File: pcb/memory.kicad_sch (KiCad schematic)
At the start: 2 parts, among them U6 MT41K256M16LY, U8 MX25L3233FZN

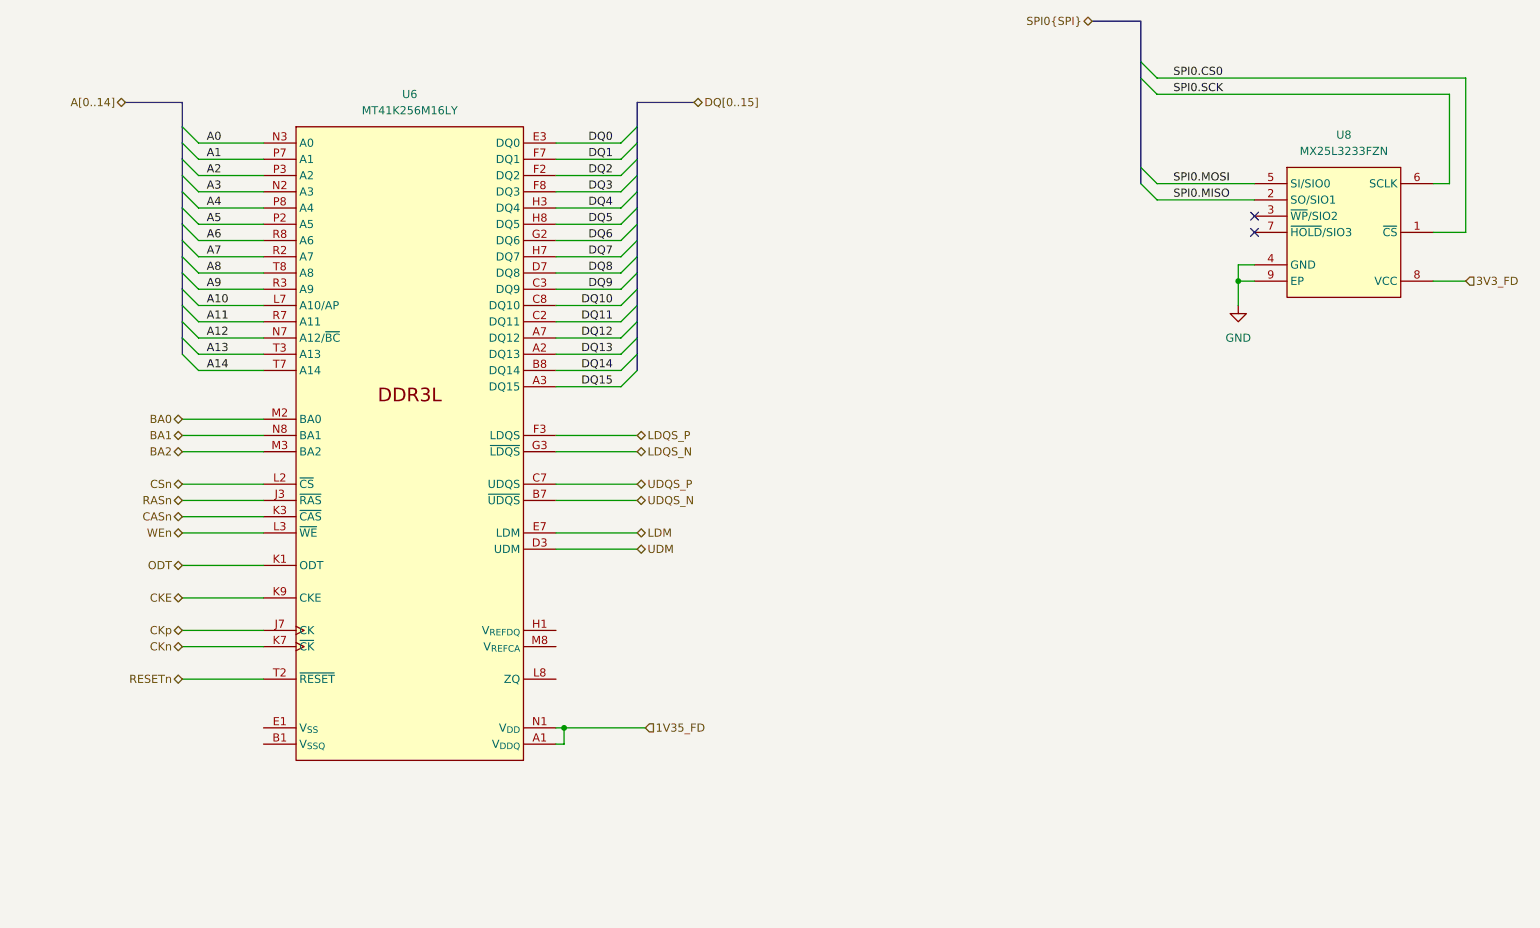
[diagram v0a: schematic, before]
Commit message: changes to power tree
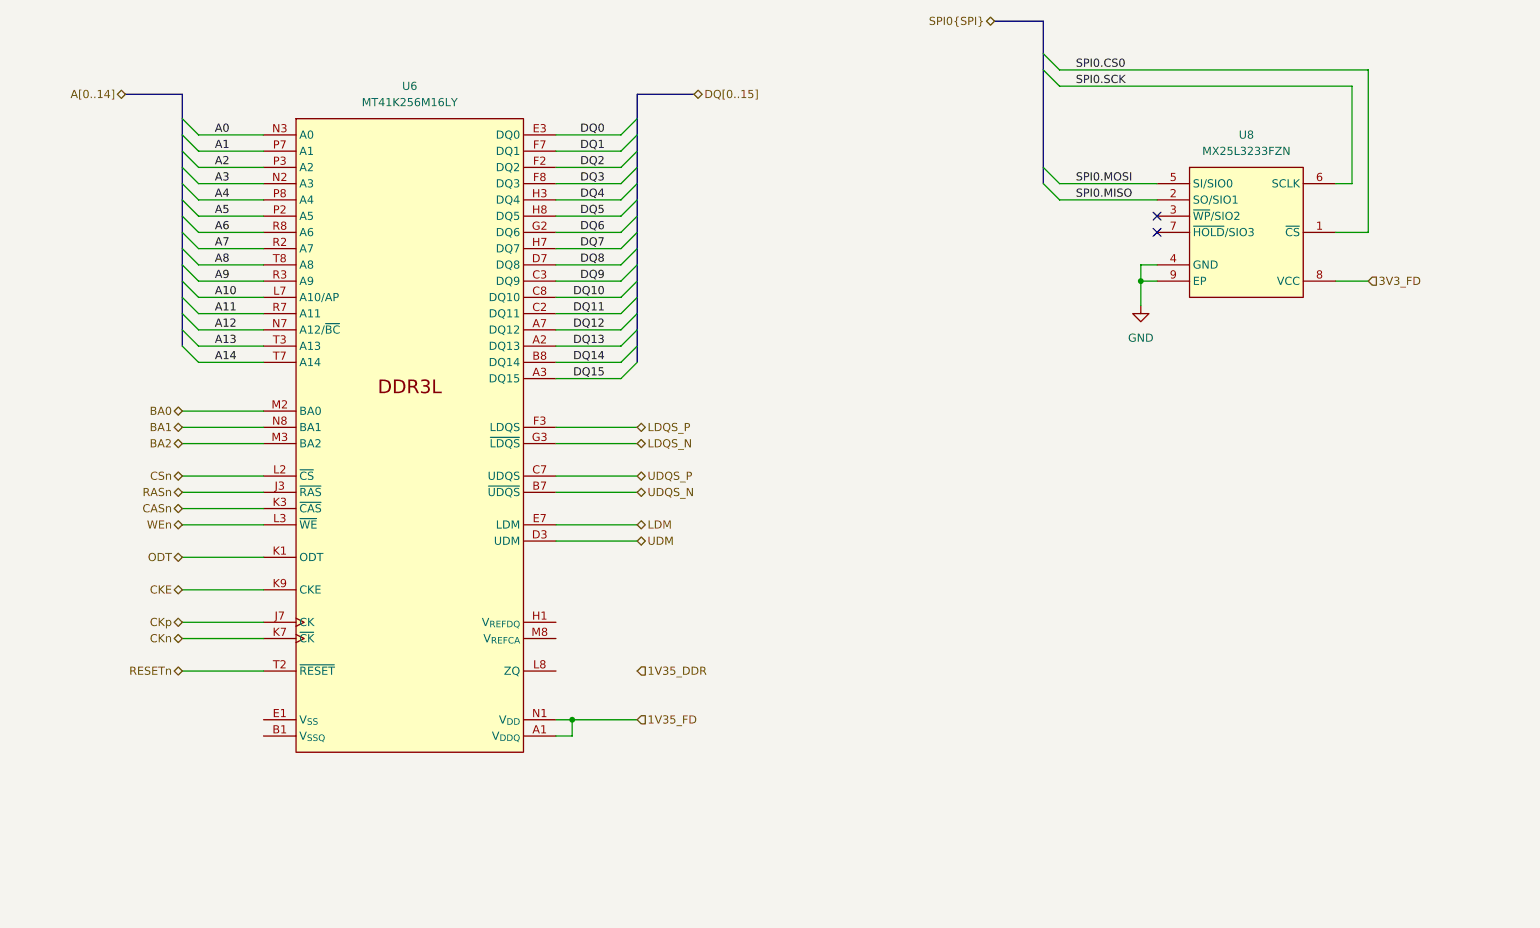
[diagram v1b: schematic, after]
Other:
- moved on the sheet: U6, U8

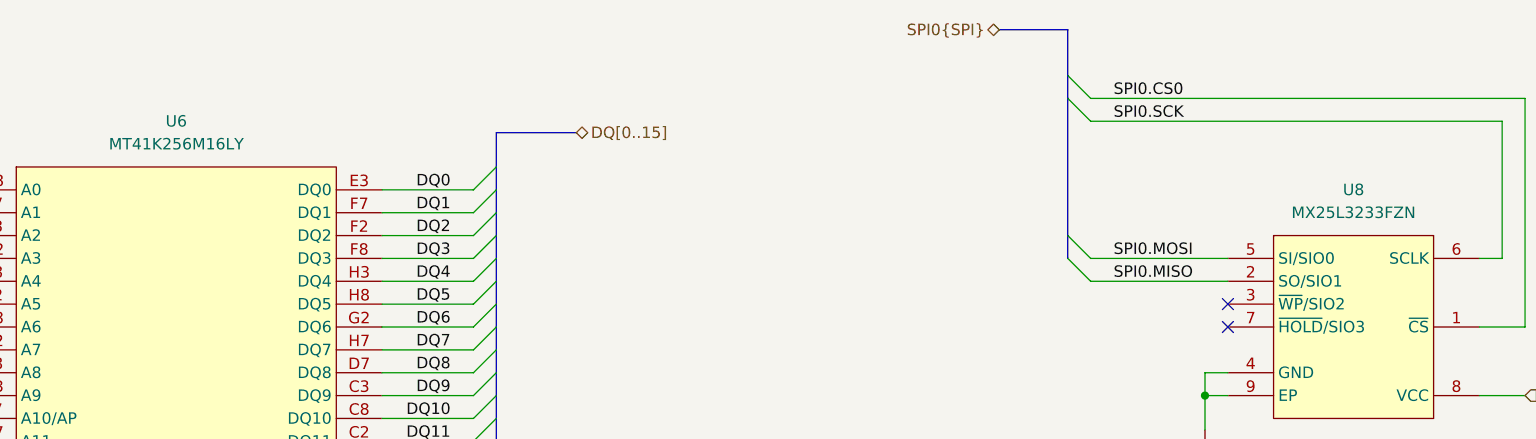
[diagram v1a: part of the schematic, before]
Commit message: moved stuff around, bom
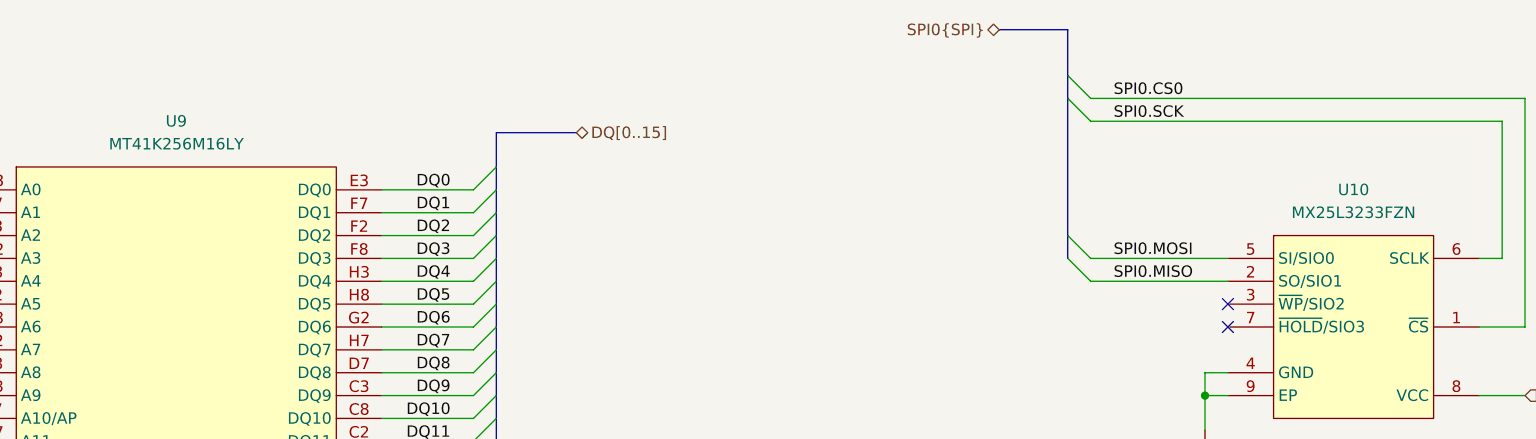
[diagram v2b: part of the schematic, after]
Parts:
- renumbered U8 to U10, U6 to U9
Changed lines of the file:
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@@
 		(dnp no)
 		(fields_autoplaced yes)
-		(property "Reference" "U8"
+		(property "Reference" "U10"
 			(at 237.49 43.18 0)
 			(effects
@@
 			(project ""
 				(path "/e63e39d7-6ac0-4ffd-8aa3-1841a4541b55/59d21473-a004-4514-8090-fd93db818925/b633a666-4c3d-4ac9-9e0f-b350177ade0b"
-					(reference "U8")
+					(reference "U10")
 					(unit 1)
 				)
@@
 		(dnp no)
 		(fields_autoplaced yes)
-		(property "Reference" "U6"
+		(property "Reference" "U9"
 			(at 106.68 35.56 0)
 			(effects
@@
 			(project ""
 				(path "/e63e39d7-6ac0-4ffd-8aa3-1841a4541b55/59d21473-a004-4514-8090-fd93db818925/b633a666-4c3d-4ac9-9e0f-b350177ade0b"
-					(reference "U6")
+					(reference "U9")
 					(unit 1)
 				)

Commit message: qspi
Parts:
- U10: value MX25L3233FZN -> MX25L12835F
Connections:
- net 1V35_FD is gone; now on net 1V35_DDR: U9.A1 (V_{DDQ}), U9.A8 (V_{DDQ}), U9.B2 (V_{DD}), U9.C1 (V_{DDQ}), U9.C9 (V_{DDQ}), U9.D2 (V_{DDQ}), U9.D9 (V_{DD}), U9.E9 (V_{DDQ}), U9.F1 (V_{DDQ}), U9.G7 (V_{DD}), U9.H2 (V_{DDQ}), U9.H9 (V_{DDQ}), U9.K2 (V_{DD}), U9.K8 (V_{DD}), U9.N1 (V_{DD}), U9.N9 (V_{DD}), U9.R1 (V_{DD}), U9.R9 (V_{DD})
- net QSPI0.SIO2: now reaches U10.3 (~{WP}/SIO2)
- net QSPI0.SIO3: now reaches U10.7 (~{HOLD}/SIO3)
- net SPI0.CS0 renamed QSPI0.CS0n
- net SPI0.MISO renamed QSPI0.SIO1
- net SPI0.MOSI renamed QSPI0.SIO0
- net SPI0.SCK renamed QSPI0.SCLK
- no-connect marks 2 -> 0
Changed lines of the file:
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@@
 		(company "Andre S Winkel")
+	)
+	(bus_alias "QSPI"
+		(members "SIO0" "SIO1" "SIO2" "SIO3" "SCLK" "CS0n" "CS1n")
 	)
 	(junction
@@
 		(color 0 0 0 0)
 	)
-	(no_connect
-		(at 223.52 58.42)
-	)
-	(no_connect
-		(at 223.52 55.88)
-	)
 	(bus_entry
 		(at 139.7 53.34)
@@
 	)
 	(bus_entry
+		(at 205.74 55.88)
+		(size 2.54 2.54)
+		(stroke
+			(width 0)
+			(type default)
+		)
+	)
+	(bus_entry
 		(at 73.66 58.42)
 		(size -2.54 -2.54)
@@
 	)
 	(bus_entry
+		(at 205.74 53.34)
+		(size 2.54 2.54)
+		(stroke
+			(width 0)
+			(type default)
+		)
+	)
+	(bus_entry
 		(at 73.66 45.72)
 		(size -2.54 -2.54)
@@
 	(wire
 		(pts
+			(xy 208.28 58.42) (xy 223.52 58.42)
+		)
+		(stroke
+			(width 0)
+			(type default)
+		)
+	)
+	(wire
+		(pts
 			(xy 71.12 121.92) (xy 83.82 121.92)
 		)
@@
 	(bus
 		(pts
+			(xy 205.74 50.8) (xy 205.74 53.34)
+		)
+		(stroke
+			(width 0)
+			(type default)
+		)
+	)
+	(bus
+		(pts
 			(xy 71.12 58.42) (xy 71.12 55.88)
 		)
@@
 		)
 	)
+	(wire
+		(pts
+			(xy 208.28 55.88) (xy 223.52 55.88)
+		)
+		(stroke
+			(width 0)
+			(type default)
+		)
+	)
 	(bus
 		(pts
@@
 		)
 	)
+	(bus
+		(pts
+			(xy 205.74 53.34) (xy 205.74 55.88)
+		)
+		(stroke
+			(width 0)
+			(type default)
+		)
+	)
 	(wire
 		(pts
@@
 		)
 	)
-	(label "SPI0.CS0"
+	(label "QSPI0.CS0n"
 		(at 210.82 33.02 0)
 		(effects
@@
 		)
 	)
-	(label "SPI0.SCK"
+	(label "QSPI0.SIO3"
+		(at 210.82 58.42 0)
+		(effects
+			(font
+				(size 1.27 1.27)
+			)
+			(justify left bottom)
+		)
+	)
+	(label "QSPI0.SIO2"
+		(at 210.82 55.88 0)
+		(effects
+			(font
+				(size 1.27 1.27)
+			)
+			(justify left bottom)
+		)
+	)
+	(label "QSPI0.SCLK"
 		(at 210.82 35.56 0)
 		(effects
@@
 		)
 	)
-	(label "SPI0.MOSI"
+	(label "QSPI0.SIO0"
 		(at 210.82 50.8 0)
 		(effects
@@
 		)
 	)
-	(label "SPI0.MISO"
+	(label "QSPI0.SIO1"
 		(at 210.82 53.34 0)
 		(effects
@@
 		)
 	)
-	(hierarchical_label "SPI0{SPI}"
+	(hierarchical_label "QSPI0{QSPI}"
 		(shape bidirectional)
 		(at 198.12 25.4 180)
@@
 		)
 	)
-	(hierarchical_label "1V35_FD"
+	(hierarchical_label "1V35_DDR"
 		(shape input)
 		(at 142.24 134.62 0)
@@
 			)
 			(justify right)
-		)
-	)
-	(hierarchical_label "1V35_DDR"
-		(shape input)
-		(at 142.24 127 0)
-		(effects
-			(font
-				(size 1.27 1.27)
-			)
-			(justify left)
 		)
 	)
@@
 			)
 		)
-		(property "Value" "MX25L3233FZN"
+		(property "Value" "MX25L12835F"
 			(at 237.49 45.72 0)
 			(effects

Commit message: bom
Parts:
- added R26: 240 1%, Resistor_SMD:R_0402_1005Metric, symbol library:R_US
- U10: Manufacturer (none) -> Macronix; Manufacturer Product Number (none) -> MX25L12835FZNI-10G; Part Description (none) -> IC FLASH 128MBIT SPI 8WSON
- U9: value MT41K256M16LY -> MT41K256M16TW-107:P TR; Manufacturer (none) -> Micron Technology Inc.; Manufacturer Product Number (none) -> MT41K256M16TW-107:P TR; Part Description (none) -> IC DRAM 4GBIT PAR 96FBGA
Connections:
- net 1V35_DDR: now also R26.2
- net GND: now also U9.A9 (V_{SS}), U9.B1 (V_{SSQ}), U9.B3 (V_{SS}), U9.B9 (V_{SSQ}), U9.D1 (V_{SSQ}), U9.D8 (V_{SSQ}), U9.E1 (V_{SS}), U9.E2 (V_{SSQ}), U9.E8 (V_{SSQ}), U9.F9 (V_{SSQ}), U9.G1 (V_{SSQ}), U9.G8 (V_{SS}), U9.G9 (V_{SSQ}), U9.J2 (V_{SS}), U9.J8 (V_{SS}), U9.M1 (V_{SS}), U9.M9 (V_{SS}), U9.P1 (V_{SS}), U9.P9 (V_{SS}), U9.T1 (V_{SS}), U9.T9 (V_{SS})
- net at U9.L8 (ZQ): now also R26.1

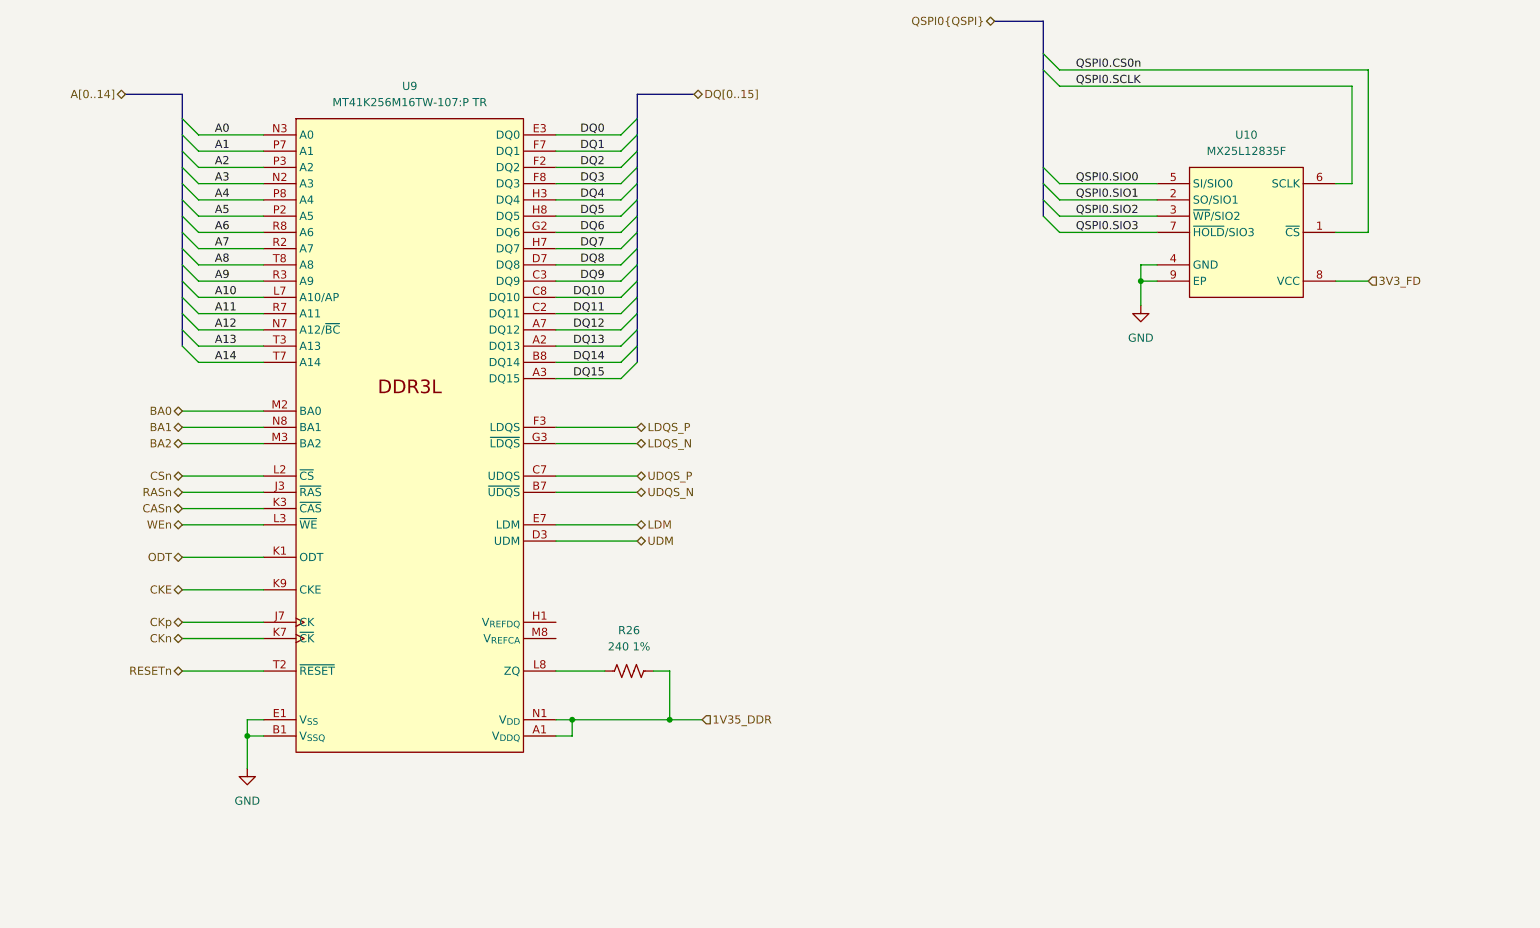
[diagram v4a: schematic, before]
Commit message: added mig ddr pinout constraints
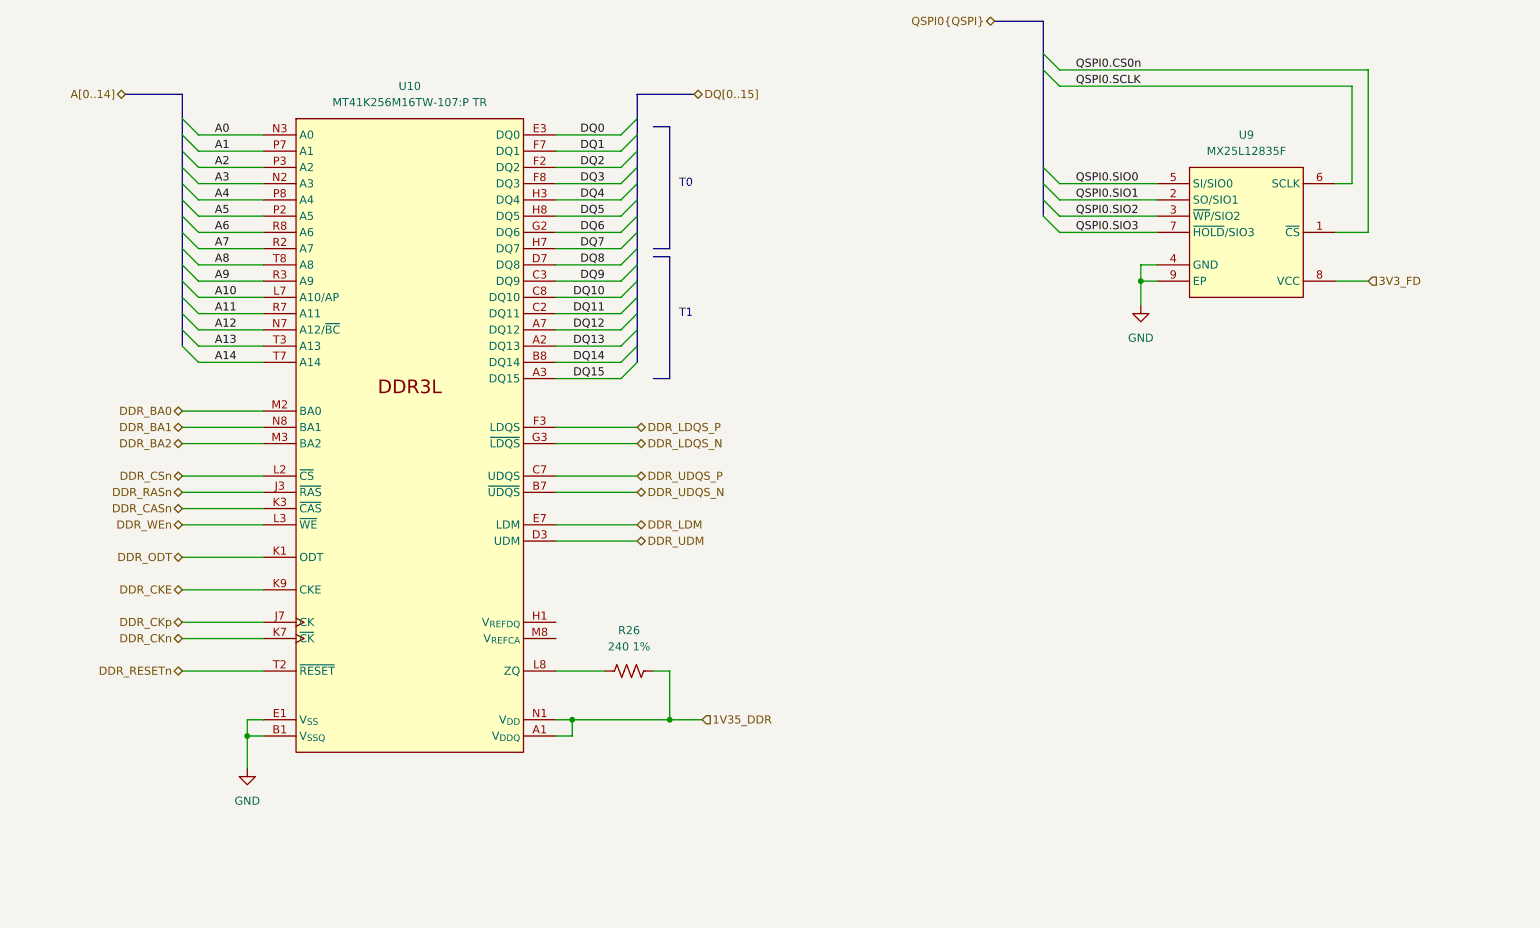
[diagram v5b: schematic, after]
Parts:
- renumbered U9 to U10, U10 to U9
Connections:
- net BA0 renamed DDR_BA0
- net BA1 renamed DDR_BA1
- net BA2 renamed DDR_BA2
- net CASn renamed DDR_CASn
- net CKE renamed DDR_CKE
- net CKn renamed DDR_CKn
- net CKp renamed DDR_CKp
- net CSn renamed DDR_CSn
- net LDM renamed DDR_LDM
- net LDQS_N renamed DDR_LDQS_N
- net LDQS_P renamed DDR_LDQS_P
- net ODT renamed DDR_ODT
- net RASn renamed DDR_RASn
- net RESETn renamed DDR_RESETn
- net UDM renamed DDR_UDM
- net UDQS_N renamed DDR_UDQS_N
- net UDQS_P renamed DDR_UDQS_P
- net WEn renamed DDR_WEn
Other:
- note added: "T0"
- note added: "T1"
